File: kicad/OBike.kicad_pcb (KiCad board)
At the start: 4 copper layers, 60 x 99.2 mm, 73 parts, among them J1 F34G-1A7Q1-E8C40, J2 Micro_SD_Card_Det1, J3 Conn_01x02, J4 Conn_01x04, J5 U.FL-R-SMT-1_10_, J6 Conn_01x02, J7 Conn_01x05, J8 Conn_01x02, Q1 SS8050, Q2 SS8050, SW1 5_position_tactile, U1 DPS368XTSA1, U10 MAX40200AUK, U2 DS3231M, U3 MCP23017_SO, U4 74HC14, U5 Seeed Studio XIAO SAMD21, U6 MAX40200AUK, U7 LC76G, U8 MAX40200AUK, U9 W25N01GVZEIG_TR

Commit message: purchased PCBs
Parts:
- removed R13: 0R, Resistor_SMD:R_0603_1608Metric
- U2: value DS3231M -> PCF8523T
- moved C1 6.00 mm to (157.1, 110.0), turned to 180 degrees
- moved C2 5.94 mm to (157.1, 108.0), turned to 180 degrees
- moved U2 0.84 mm to (158.9, 104.1)
- moved C10 0.34 mm to (128.0, 118.6)
- moved C9 0.20 mm to (147.6, 120.2)
- moved C4 0.16 mm to (130.8, 91.7)
- moved C3 0.11 mm to (130.8, 93.7)
- moved C13 0.10 mm to (172.1, 94.4)
- moved C7 0.07 mm to (140.9, 119.0)
- moved C6 0.06 mm to (141.1, 125.5)
- moved C11 0.05 mm to (125.2, 105.5)
- moved C8 0.05 mm to (147.4, 127.0)
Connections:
- U2 pad 2: 3V3 -> unconnected-(U11-OSCO-Pad2)
- U2 pad 4: Net-(U2-~{RST}) -> GND
- U2 pad 5: GND -> SDA
- U2 pad 6: unconnected-(U2-VBAT-Pad6) -> SCL
- U2 pad 7: SDA -> unconnected-(U11-~{INT1}/CLKOUT-Pad7)
- U2 pad 8: SCL -> 3V3
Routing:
- net GND: track 96.9 -> 99.8 mm, vias 60 -> 61
- net Net-(U2-~{RST}): track 2.03 -> 0.00 mm
- net SDA: track 89.9 -> 88.4 mm
- net SCL: track 85.5 -> 84.1 mm
- net SCR_BK: track 62.3 -> 63.1 mm
- net 3V3: track 42.9 -> 42.2 mm, vias 16 -> 15

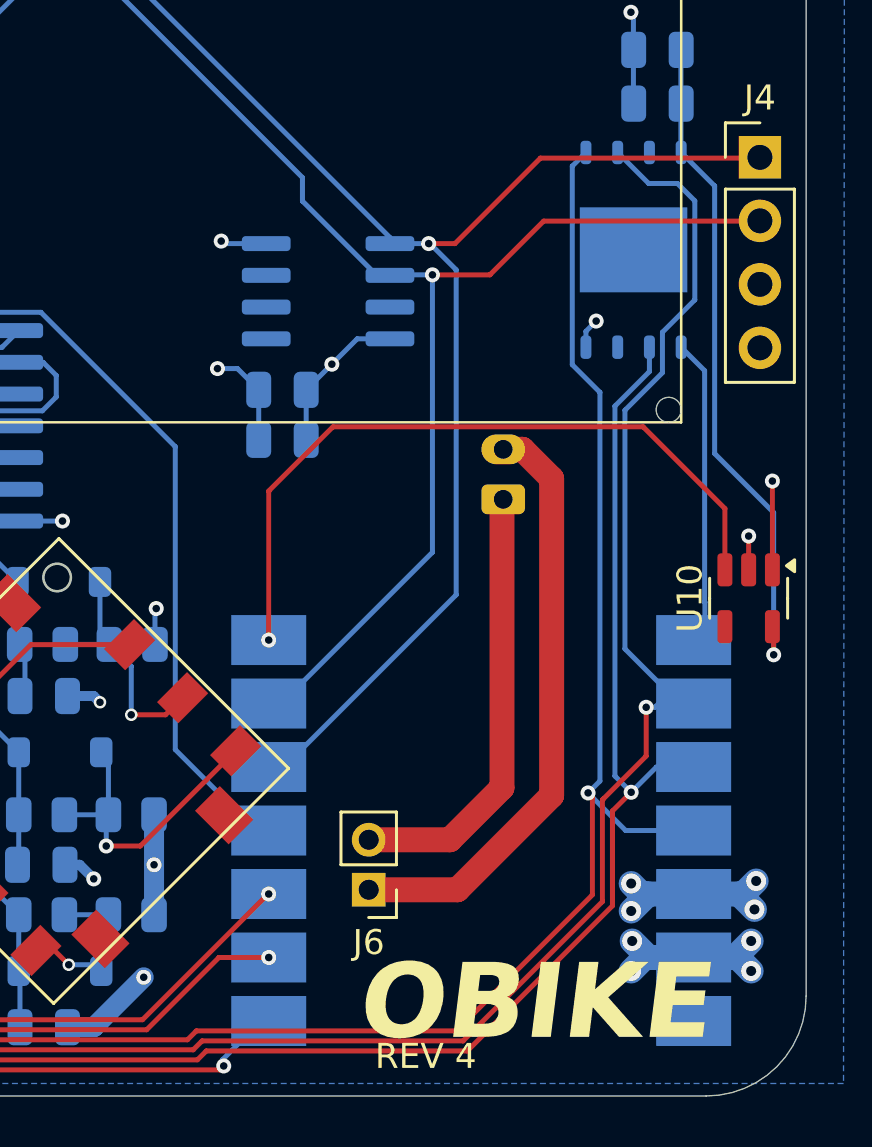
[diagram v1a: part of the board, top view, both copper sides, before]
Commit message: pcb fixes
- WP and Hold pins on flash shorted to aux 3v3
- added a 32.768khz crystal for the RTC
- fixed wrong part numbers for Q1 & Q2
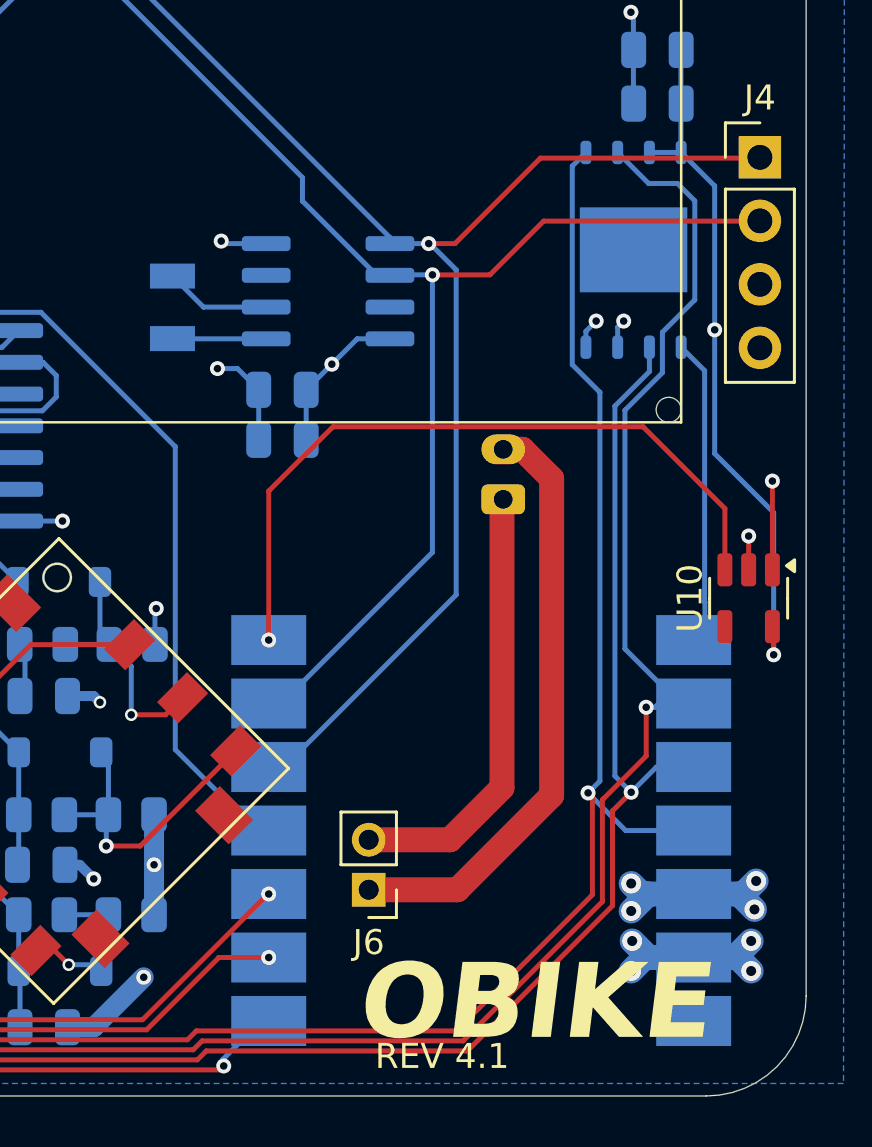
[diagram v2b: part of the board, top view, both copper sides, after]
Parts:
- added Y1: Crystal, Jauch:OSCSC320X150X90, B.Cu at (152.7, 104.7)
- U2: value PCF8523T -> PCF85063AT
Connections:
- U2 pad 1: unconnected-(U11-OSCI-Pad1) -> Net-(U2-OSCI)
- U2 pad 2: unconnected-(U11-OSCO-Pad2) -> Net-(U2-OSCO)
- U9 pad 3: unconnected-(U9-/WP(IO2)-Pad3) -> AUX_3V3
- U9 pad 7: unconnected-(U9-/HOLD(IO3)-Pad7) -> AUX_3V3
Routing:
- net AUX_3V3: track 245.6 -> 251.8 mm, vias 6 -> 8
- net Net-(U2-OSCO): track 0.00 -> 4.26 mm
- net Net-(U2-OSCI): track 0.00 -> 3.75 mm
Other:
- board text added: "REV 4.1"
- board text removed: "REV 4"

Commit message: ui updates
- also disp reset working
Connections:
- J1 pad 15: unconnected-(J1-Pad15) -> SCR_RST
- U3 pad 8: unconnected-(U3-GPB7-Pad8) -> SCR_RST
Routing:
- net SCR_RST: track 0.00 -> 112.3 mm
- net /BAT-: track 24.0 -> 22.0 mm
- net /BAT+: track 17.8 -> 15.9 mm
